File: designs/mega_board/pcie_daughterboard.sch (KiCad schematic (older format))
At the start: 13 parts

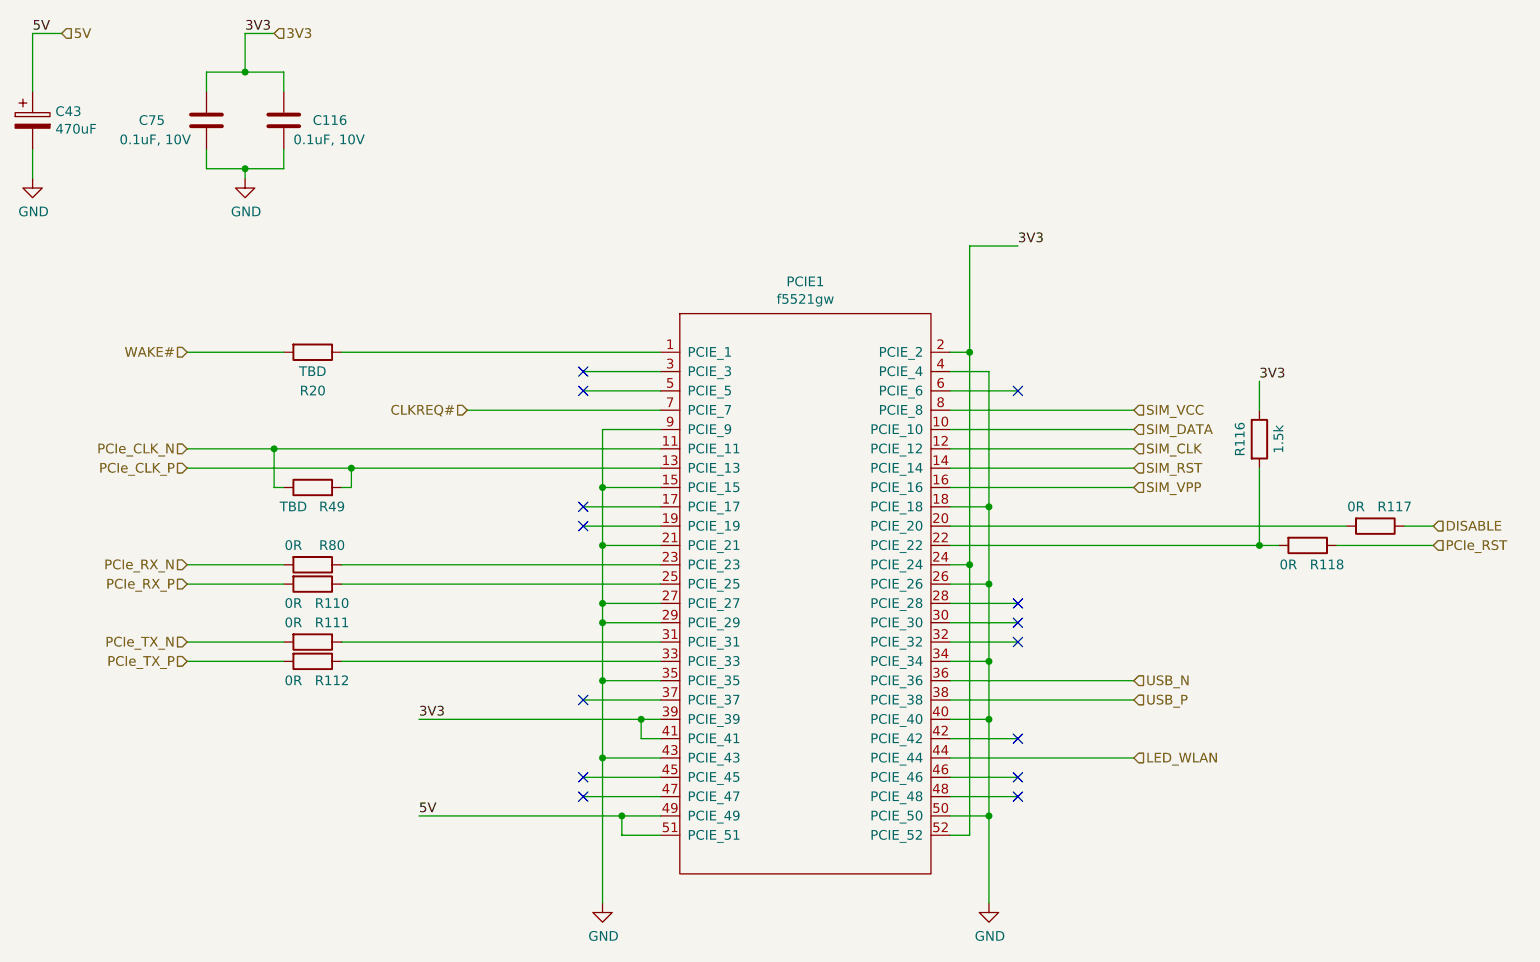
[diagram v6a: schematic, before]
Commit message: Add BOM definition to all resistors
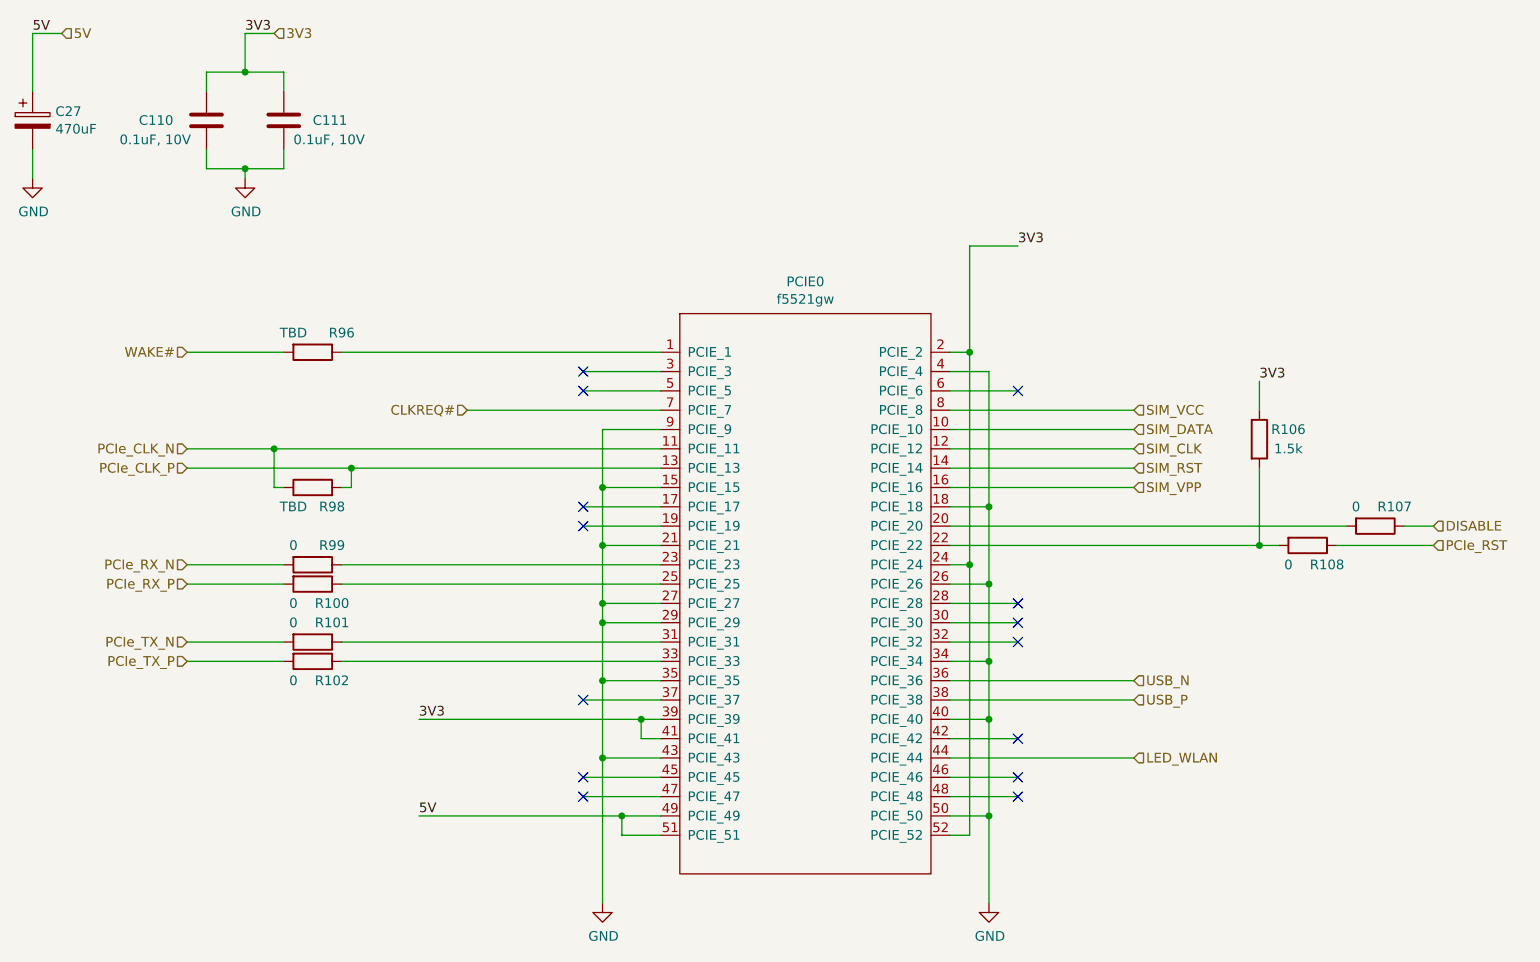
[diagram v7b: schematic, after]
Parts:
- R100, R101, R102, R107, R108, R99: value 0R -> 0; Manufacturer (none) -> Panasonic Electronic Components; Manufacturer PN (none) -> ERJ-2GE0R00X; Supplier (none) -> DigiKey; Supplier PN (none) -> P0.0JDKR-ND
- R106: Manufacturer (none) -> Panasonic Electronic Components; Manufacturer PN (none) -> ERJ-PA2F1501X; Supplier (none) -> DigiKey; Supplier PN (none) -> P17225DKR-ND
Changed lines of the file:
@@
 $Descr A4 11693 8268
 encoding utf-8
-Sheet 13 14
+Sheet 11 14
 Title "LibreRouter - Megaboard"
 Date "2019-06-26"
@@
 AR Path="/5D1650F5/5D19C7E9" Ref="PCIE1"  Part="1"
 AR Path="/5D19C7E9" Ref="U?"  Part="1"
-F 0 "PCIE1" H 5700 5865 50  0000 C CNN
+F 0 "PCIE0" H 5700 5865 50  0000 C CNN
 F 1 "f5521gw" H 5700 5774 50  0000 C CNN
 F 2 "LibreRouter_MegaBoard:MINI-PCI-E-FULL" H 5700 4250 50  0001 C CNN
@@
 AR Path="/5D032C97/5D19F8AF" Ref="#PWR0173"  Part="1"
 AR Path="/5D1650F5/5D19F8AF" Ref="#PWR0190"  Part="1"
-F 0 "#PWR0190" H 6650 5600 50  0001 C CNN
+F 0 "#PWR0173" H 6650 5600 50  0001 C CNN
 F 1 "GND" H 6655 5677 50  0000 C CNN
 F 2 "" H 6650 5850 50  0001 C CNN
@@
 AR Path="/5D032C97/5D1A0459" Ref="R108"  Part="1"
 AR Path="/5D1650F5/5D1A0459" Ref="R118"  Part="1"
-F 0 "R118" V 8400 4100 50  0000 C CNN
-F 1 "0R" V 8400 3900 50  0000 C CNN
+F 0 "R108" V 8400 4100 50  0000 C CNN
+F 1 "0" V 8400 3900 50  0000 C CNN
 F 2 "LibreRouter_MegaBoard:R0402" V 8230 4000 50  0001 C CNN
 F 3 "~" H 8300 4000 50  0001 C CNN
+F 4 "Panasonic Electronic Components" H 8300 4000 50  0001 C CNN "Manufacturer"
+F 5 "ERJ-2GE0R00X" H 8300 4000 50  0001 C CNN "Manufacturer PN"
+F 6 "DigiKey" H 8300 4000 50  0001 C CNN "Supplier"
+F 7 "P0.0JDKR-ND" H 8300 4000 50  0001 C CNN "Supplier PN"
 	1    8300 4000
 	0    1    1    0
@@
 AR Path="/5D032C97/5D1A04F3" Ref="R107"  Part="1"
 AR Path="/5D1650F5/5D1A04F3" Ref="R117"  Part="1"
-F 0 "R117" V 8550 4000 50  0000 C CNN
-F 1 "0R" V 8550 3800 50  0000 C CNN
+F 0 "R107" V 8550 4000 50  0000 C CNN
+F 1 "0" V 8550 3800 50  0000 C CNN
 F 2 "LibreRouter_MegaBoard:R0402" V 8580 3900 50  0001 C CNN
 F 3 "~" H 8650 3900 50  0001 C CNN
+F 4 "Panasonic Electronic Components" H 8650 3900 50  0001 C CNN "Manufacturer"
+F 5 "ERJ-2GE0R00X" H 8650 3900 50  0001 C CNN "Manufacturer PN"
+F 6 "DigiKey" H 8650 3900 50  0001 C CNN "Supplier"
+F 7 "P0.0JDKR-ND" H 8650 3900 50  0001 C CNN "Supplier PN"
 	1    8650 3900
 	0    1    1    0
@@
 AR Path="/5D032C97/5D1A051B" Ref="R106"  Part="1"
 AR Path="/5D1650F5/5D1A051B" Ref="R116"  Part="1"
-F 0 "R116" V 7950 3450 50  0000 C CNN
-F 1 "1.5k" V 8150 3450 50  0000 C CNN
+F 0 "R106" H 8200 3500 50  0000 C CNN
+F 1 "1.5k" H 8200 3400 50  0000 C CNN
 F 2 "LibreRouter_MegaBoard:R0402" V 7980 3450 50  0001 C CNN
 F 3 "~" H 8050 3450 50  0001 C CNN
+F 4 "Panasonic Electronic Components" H 8050 3450 50  0001 C CNN "Manufacturer"
+F 5 "ERJ-PA2F1501X" H 8050 3450 50  0001 C CNN "Manufacturer PN"
+F 6 "DigiKey" H 8050 3450 50  0001 C CNN "Supplier"
+F 7 "P17225DKR-ND" H 8050 3450 50  0001 C CNN "Supplier PN"
 	1    8050 3450
 	1    0    0    -1
@@
 AR Path="/5D032C97/5D1A5891" Ref="R96"  Part="1"
 AR Path="/5D1650F5/5D1A5891" Ref="R20"  Part="1"
-F 0 "R20" V 3350 3000 50  0000 C CNN
-F 1 "TBD" V 3250 3000 50  0000 C CNN
+F 0 "R96" V 3050 3150 50  0000 C CNN
+F 1 "TBD" V 3050 2900 50  0000 C CNN
 F 2 "LibreRouter_MegaBoard:R0402" V 3080 3000 50  0001 C CNN
 F 3 "~" H 3150 3000 50  0001 C CNN
@@
 AR Path="/5D032C97/5D1AF5AD" Ref="R98"  Part="1"
 AR Path="/5D1650F5/5D1AF5AD" Ref="R49"  Part="1"
-F 0 "R49" V 3050 3600 50  0000 C CNN
+F 0 "R98" V 3050 3600 50  0000 C CNN
 F 1 "TBD" V 3050 3800 50  0000 C CNN
 F 2 "LibreRouter_MegaBoard:R0402" V 3080 3700 50  0001 C CNN
@@
 AR Path="/5D032C97/5D1C5785" Ref="C110"  Part="1"
 AR Path="/5D1650F5/5D1C5785" Ref="C75"  Part="1"
-F 0 "C75" H 2250 1800 50  0000 L CNN
+F 0 "C110" H 2250 1800 50  0000 L CNN
 F 1 "0.1uF, 10V" H 2150 1700 50  0000 L CNN
 F 2 "LibreRouter_MegaBoard:C0402" H 2638 1650 50  0001 C CNN
@@
 AR Path="/5D032C97/5D1C583F" Ref="C111"  Part="1"
 AR Path="/5D1650F5/5D1C583F" Ref="C116"  Part="1"
-F 0 "C116" H 3150 1800 50  0000 L CNN
+F 0 "C111" H 3150 1800 50  0000 L CNN
 F 1 "0.1uF, 10V" H 3050 1700 50  0000 L CNN
 F 2 "LibreRouter_MegaBoard:C0402" H 3038 1650 50  0001 C CNN
@@
 AR Path="/5D032C97/5D1C58DE" Ref="#PWR0174"  Part="1"
 AR Path="/5D1650F5/5D1C58DE" Ref="#PWR0191"  Part="1"
-F 0 "#PWR0191" H 2800 1850 50  0001 C CNN
+F 0 "#PWR0174" H 2800 1850 50  0001 C CNN
 F 1 "GND" H 2805 1927 50  0000 C CNN
 F 2 "" H 2800 2100 50  0001 C CNN
@@
 AR Path="/5D032C97/5D1D537C" Ref="#PWR0175"  Part="1"
 AR Path="/5D1650F5/5D1D537C" Ref="#PWR0192"  Part="1"
-F 0 "#PWR0192" H 1700 1850 50  0001 C CNN
+F 0 "#PWR0175" H 1700 1850 50  0001 C CNN
 F 1 "GND" H 1705 1927 50  0000 C CNN
 F 2 "" H 1700 2100 50  0001 C CNN
@@
 AR Path="/5D032C97/5D1D8CB3" Ref="C27"  Part="1"
 AR Path="/5D1650F5/5D1D8CB3" Ref="C43"  Part="1"
-F 0 "C43" H 1818 1846 50  0000 L CNN
+F 0 "C27" H 1818 1846 50  0000 L CNN
 F 1 "470uF" H 1818 1755 50  0000 L CNN
 F 2 "LibreRouter_MegaBoard:UD-6,3X7,7_NICHICON" H 1738 1650 50  0001 C CNN
@@
 AR Path="/5D032C97/5D1F3D95" Ref="R99"  Part="1"
 AR Path="/5D1650F5/5D1F3D95" Ref="R80"  Part="1"
-F 0 "R80" V 3050 4200 50  0000 C CNN
-F 1 "0R" V 3050 4000 50  0000 C CNN
+F 0 "R99" V 3050 4200 50  0000 C CNN
+F 1 "0" V 3050 4000 50  0000 C CNN
 F 2 "LibreRouter_MegaBoard:R0402" V 3080 4100 50  0001 C CNN
 F 3 "~" H 3150 4100 50  0001 C CNN
+F 4 "Panasonic Electronic Components" H 3150 4100 50  0001 C CNN "Manufacturer"
+F 5 "ERJ-2GE0R00X" H 3150 4100 50  0001 C CNN "Manufacturer PN"
+F 6 "DigiKey" H 3150 4100 50  0001 C CNN "Supplier"
+F 7 "P0.0JDKR-ND" H 3150 4100 50  0001 C CNN "Supplier PN"
 	1    3150 4100
 	0    1    1    0
@@
 AR Path="/5D032C97/5D1F3F5D" Ref="R100"  Part="1"
 AR Path="/5D1650F5/5D1F3F5D" Ref="R110"  Part="1"
-F 0 "R110" V 3250 4300 50  0000 C CNN
-F 1 "0R" V 3250 4100 50  0000 C CNN
+F 0 "R100" V 3250 4300 50  0000 C CNN
+F 1 "0" V 3250 4100 50  0000 C CNN
 F 2 "LibreRouter_MegaBoard:R0402" V 3080 4200 50  0001 C CNN
 F 3 "~" H 3150 4200 50  0001 C CNN
+F 4 "Panasonic Electronic Components" H 3150 4200 50  0001 C CNN "Manufacturer"
+F 5 "ERJ-2GE0R00X" H 3150 4200 50  0001 C CNN "Manufacturer PN"
+F 6 "DigiKey" H 3150 4200 50  0001 C CNN "Supplier"
+F 7 "P0.0JDKR-ND" H 3150 4200 50  0001 C CNN "Supplier PN"
 	1    3150 4200
 	0    1    1    0
@@
 AR Path="/5D032C97/5D1F7584" Ref="R101"  Part="1"
 AR Path="/5D1650F5/5D1F7584" Ref="R111"  Part="1"
-F 0 "R111" V 3050 4600 50  0000 C CNN
-F 1 "0R" V 3050 4400 50  0000 C CNN
+F 0 "R101" V 3050 4600 50  0000 C CNN
+F 1 "0" V 3050 4400 50  0000 C CNN
 F 2 "LibreRouter_MegaBoard:R0402" V 3080 4500 50  0001 C CNN
 F 3 "~" H 3150 4500 50  0001 C CNN
+F 4 "Panasonic Electronic Components" H 3150 4500 50  0001 C CNN "Manufacturer"
+F 5 "ERJ-2GE0R00X" H 3150 4500 50  0001 C CNN "Manufacturer PN"
+F 6 "DigiKey" H 3150 4500 50  0001 C CNN "Supplier"
+F 7 "P0.0JDKR-ND" H 3150 4500 50  0001 C CNN "Supplier PN"
 	1    3150 4500
 	0    1    1    0
@@
 AR Path="/5D032C97/5D1F758C" Ref="R102"  Part="1"
 AR Path="/5D1650F5/5D1F758C" Ref="R112"  Part="1"
-F 0 "R112" V 3250 4700 50  0000 C CNN
-F 1 "0R" V 3250 4500 50  0000 C CNN
+F 0 "R102" V 3250 4700 50  0000 C CNN
+F 1 "0" V 3250 4500 50  0000 C CNN
 F 2 "LibreRouter_MegaBoard:R0402" V 3080 4600 50  0001 C CNN
 F 3 "~" H 3150 4600 50  0001 C CNN
+F 4 "Panasonic Electronic Components" H 3150 4600 50  0001 C CNN "Manufacturer"
+F 5 "ERJ-2GE0R00X" H 3150 4600 50  0001 C CNN "Manufacturer PN"
+F 6 "DigiKey" H 3150 4600 50  0001 C CNN "Supplier"
+F 7 "P0.0JDKR-ND" H 3150 4600 50  0001 C CNN "Supplier PN"
 	1    3150 4600
 	0    1    1    0
@@
 AR Path="/5D032C97/5D20ABC1" Ref="#PWR0176"  Part="1"
 AR Path="/5D1650F5/5D20ABC1" Ref="#PWR0193"  Part="1"
-F 0 "#PWR0193" H 4650 5600 50  0001 C CNN
+F 0 "#PWR0176" H 4650 5600 50  0001 C CNN
 F 1 "GND" H 4655 5677 50  0000 C CNN
 F 2 "" H 4650 5850 50  0001 C CNN

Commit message: Add BOM definition for components. We need more iformation for all the components that are not defined.
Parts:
- PCIE0: Manufacturer (none) -> Molex; Manufacturer PN (none) -> 0679105700; Supplier (none) -> DigiKey; Supplier PN (none) -> WM7125DKR-ND
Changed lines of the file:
@@
 F 2 "LibreRouter_MegaBoard:MINI-PCI-E-FULL" H 5700 4250 50  0001 C CNN
 F 3 "" H 5700 4250 50  0001 C CNN
+F 4 "Molex" H 5700 4250 50  0001 C CNN "Manufacturer"
+F 5 "0679105700" H 5700 4250 50  0001 C CNN "Manufacturer PN"
+F 6 "DigiKey" H 5700 4250 50  0001 C CNN "Supplier"
+F 7 "WM7125DKR-ND" H 5700 4250 50  0001 C CNN "Supplier PN"
 	1    5700 4250
 	1    0    0    -1
